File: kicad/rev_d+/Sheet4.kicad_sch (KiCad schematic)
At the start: 38 parts, among them J2 JUMPER, J3 JUMPER, X26 ext. video/sound, X7 DB15VGA, X8 PLB1-4I, X9 PLB1-2

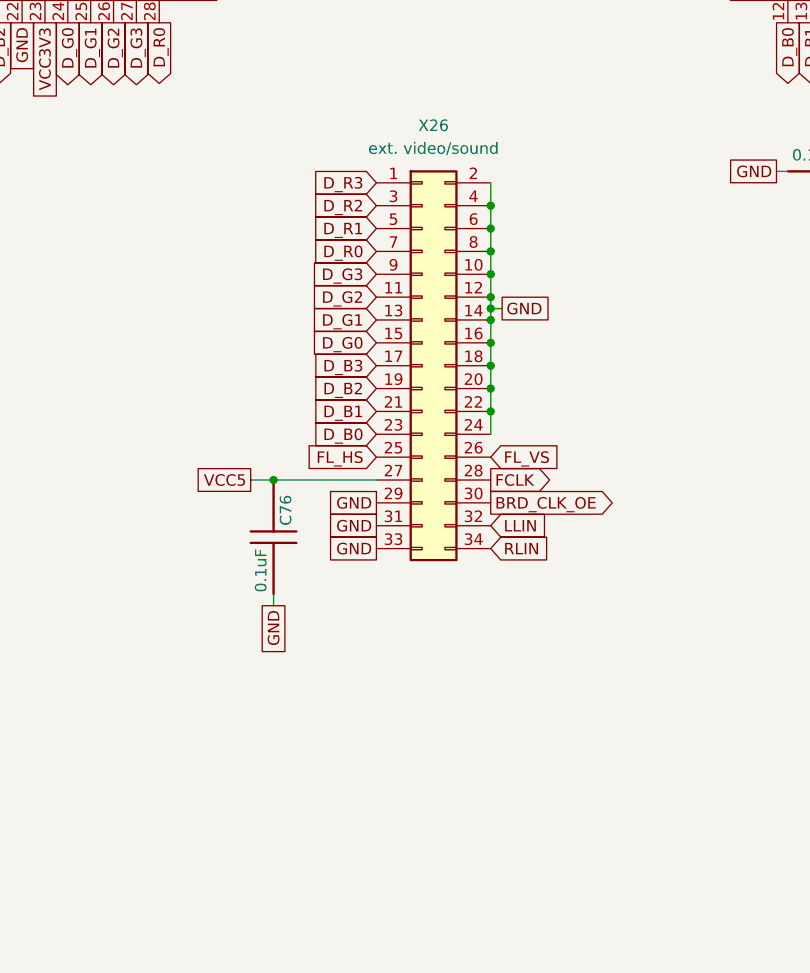
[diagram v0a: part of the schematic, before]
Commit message: pentevo: rev D+: add I2C ext. connector, update HDMI mezzanine board connector with analog power and I2C
git-svn-id: svn://localhost/local-pentevo@1353 c6c76956-fad2-4150-a3a9-ea0a427205ba
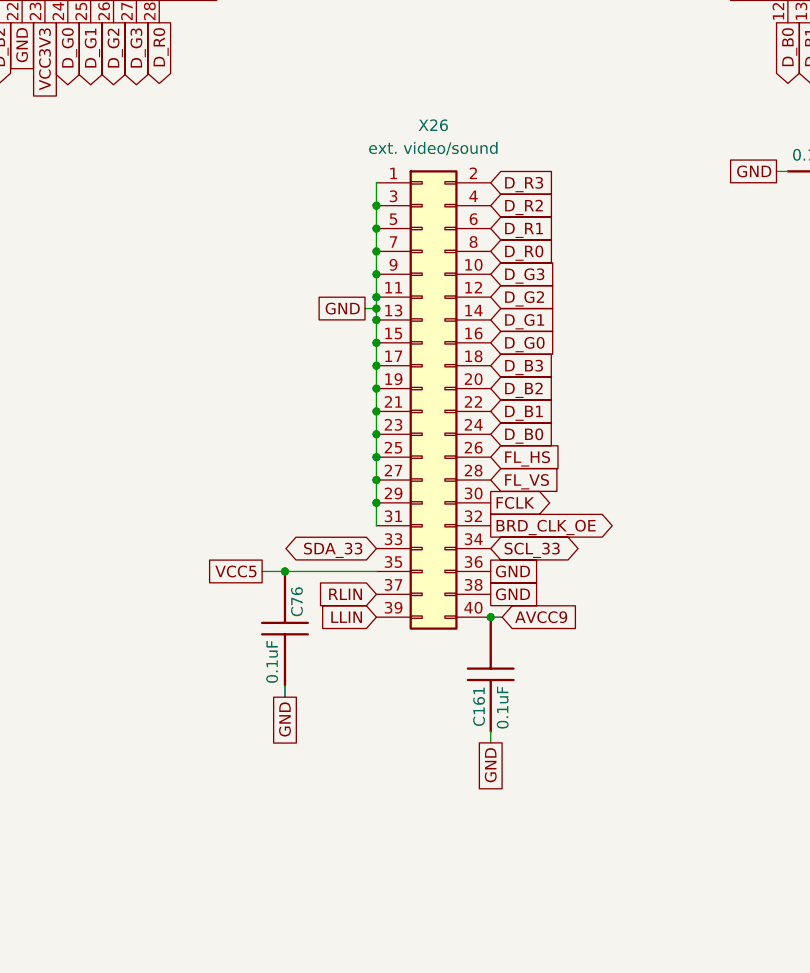
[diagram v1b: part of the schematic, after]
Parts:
- added C161: 0.1uF, C-CHIP, symbol eva-altium-import:Sheet1_3_CAPCHIP
- X26: symbol Connector_Generic:Conn_02x17_Odd_Even -> Connector_Generic:Conn_02x20_Odd_Even
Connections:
- net BRD_CLK_OE: now also X26.32 (Pin_32); no longer X26.30 (Pin_30)
- net D_B0: now also X26.24 (Pin_24); no longer X26.23 (Pin_23)
- net D_B1: now also X26.22 (Pin_22); no longer X26.21 (Pin_21)
- net D_B2: now also X26.20 (Pin_20); no longer X26.19 (Pin_19)
- net D_B3: now also X26.18 (Pin_18); no longer X26.17 (Pin_17)
- net D_G0: now also X26.16 (Pin_16); no longer X26.15 (Pin_15)
- net D_G1: now also X26.14 (Pin_14); no longer X26.13 (Pin_13)
- net D_G2: now also X26.12 (Pin_12); no longer X26.11 (Pin_11)
- net D_G3: now also X26.10 (Pin_10); no longer X26.9 (Pin_9)
- net D_R0: now also X26.8 (Pin_8); no longer X26.7 (Pin_7)
- net D_R1: now also X26.6 (Pin_6); no longer X26.5 (Pin_5)
- net D_R2: now also X26.4 (Pin_4); no longer X26.3 (Pin_3)
- net D_R3: now also X26.2 (Pin_2); no longer X26.1 (Pin_1)
- net FCLK: now also X26.30 (Pin_30); no longer X26.28 (Pin_28)
- net FL_HS: now also X26.26 (Pin_26); no longer X26.25 (Pin_25)
- net FL_VS: now also X26.28 (Pin_28); no longer X26.26 (Pin_26)
- net GND: now also X26.1 (Pin_1), X26.11 (Pin_11), X26.13 (Pin_13), X26.15 (Pin_15), X26.17 (Pin_17), X26.19 (Pin_19), X26.21 (Pin_21), X26.23 (Pin_23), X26.25 (Pin_25), X26.27 (Pin_27), X26.3 (Pin_3), X26.36 (Pin_36), X26.38 (Pin_38), X26.5 (Pin_5), X26.7 (Pin_7), X26.9 (Pin_9), C161.2; no longer X26.10 (Pin_10), X26.12 (Pin_12), X26.14 (Pin_14), X26.16 (Pin_16), X26.18 (Pin_18), X26.2 (Pin_2), X26.20 (Pin_20), X26.22 (Pin_22), X26.24 (Pin_24), X26.33 (Pin_33), X26.4 (Pin_4), X26.6 (Pin_6), X26.8 (Pin_8)
- net LLIN: now also X26.39 (Pin_39); no longer X26.32 (Pin_32)
- net RLIN: now also X26.37 (Pin_37); no longer X26.34 (Pin_34)
- net VCC5: now also X26.35 (Pin_35); no longer X26.27 (Pin_27)
- new net AVCC9: C161.1, X26.40 (Pin_40)
- new net SCL_33: X26.34 (Pin_34)
- new net SDA_33: X26.33 (Pin_33)
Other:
- moved on the sheet: C76
